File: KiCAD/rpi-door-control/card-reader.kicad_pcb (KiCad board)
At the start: 2 copper layers, 62 x 15 mm, 7 parts, among them P5 CONN_4, P7 CONN_6, U1 BUZZER

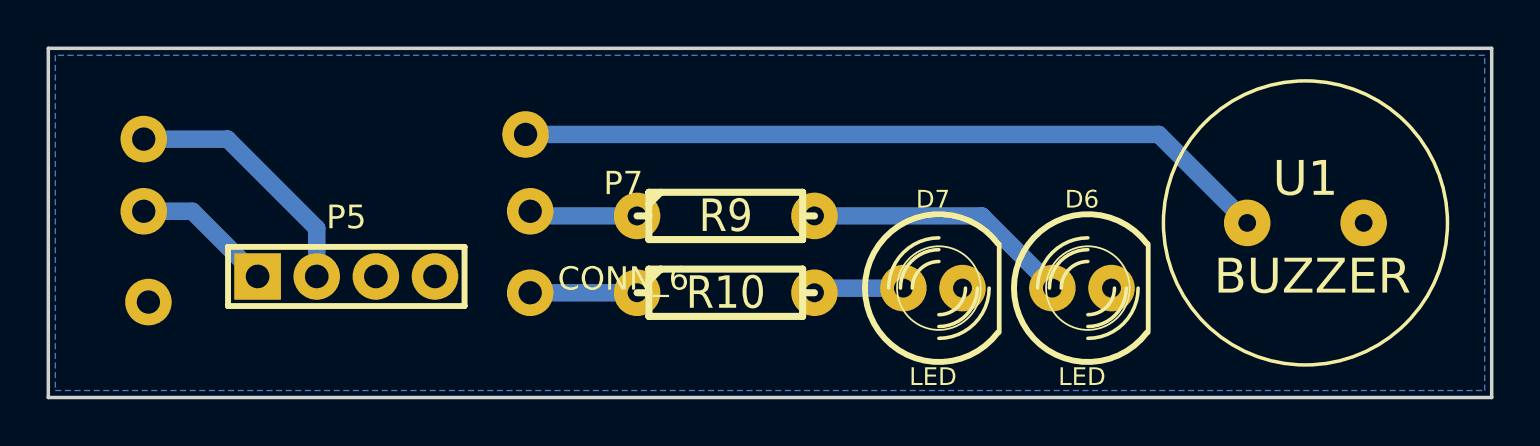
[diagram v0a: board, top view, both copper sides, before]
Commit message: cleaned up wire holes footprint
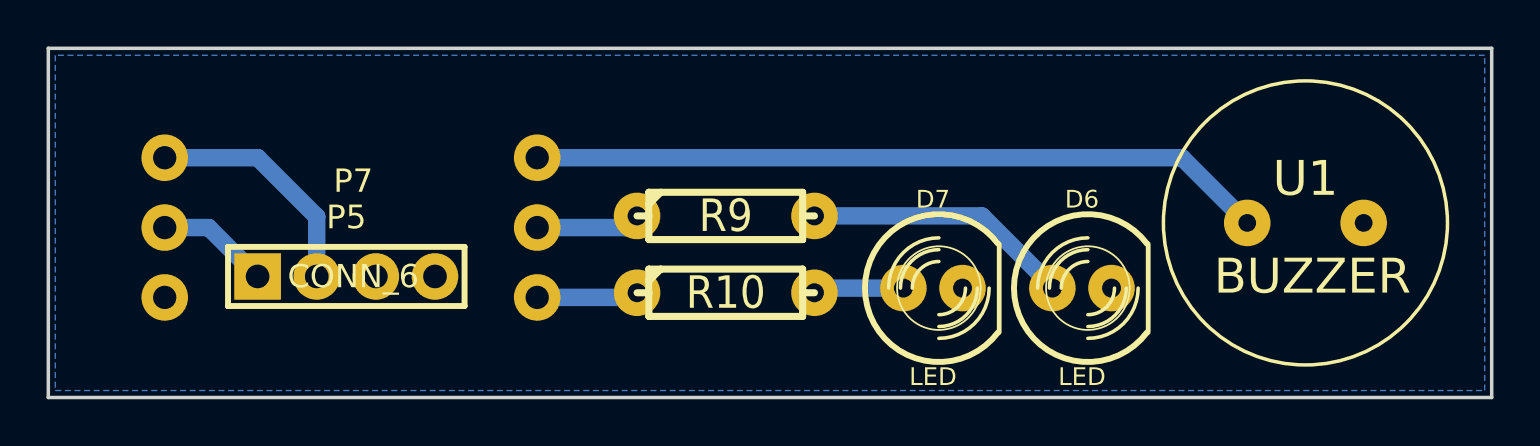
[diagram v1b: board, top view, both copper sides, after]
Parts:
- moved P7 11.6 mm to (94.7, 89.2)
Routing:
- net +5V: track 6.05 -> 4.86 mm
- net /RFID TXD: track 11.1 -> 10.1 mm
- net /BELL: track 32.6 -> 31.7 mm
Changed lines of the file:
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@@
     (thickness 1.6)
     (drawings 4)
-    (tracks 15)
+    (tracks 16)
     (zones 0)
     (modules 7)
@@
   (title_block
     (title "Card Reader Board")
-    (rev 0.3)
+    (rev 0.3.1)
     (company SBW)
     (comment 1 "To be used with Parallax serial RFID reader")
@@
     (mod_text_width 0.15)
     (pad_size 2 2)
-    (pad_drill 1.016)
+    (pad_drill 1)
     (pad_to_mask_clearance 0)
     (aux_axis_origin 72.7 73.5)
@@
     )
   )
-  (module WIRE_HOLES_6 (layer F.Cu)
-    (at 106.3 89.3)
-    (fp_text reference P7 (at 0.1 -2) (layer F.SilkS)
-      (effects (font (size 1 1) (thickness 0.15)))
-    )
-    (fp_text value CONN_6 (at 0.1 2.1) (layer F.SilkS)
-      (effects (font (size 1 1) (thickness 0.15)))
-    )
-    (pad 1 thru_hole circle (at -20.5 -0.8) (size 2 2) (drill 1)
-      (layers *.Cu *.Mask F.SilkS)
-      (net 1 +5V)
-    )
-    (pad 2 thru_hole circle (at -3.9 -0.8) (size 2 2) (drill 1)
-      (layers *.Cu *.Mask F.SilkS)
-      (net 4 /RED)
-    )
-    (pad 4 thru_hole circle (at -20.5 -3.9) (size 2 2) (drill 1)
-      (layers *.Cu *.Mask F.SilkS)
-      (net 5 "/RFID TXD")
-    )
-    (pad 3 thru_hole circle (at -3.9 2.7) (size 2 2) (drill 1)
-      (layers *.Cu *.Mask F.SilkS)
-      (net 3 /GREEN)
-    )
-    (pad 6 thru_hole circle (at -20.3 3.1) (size 2 2) (drill 1)
-      (layers *.Cu *.Mask F.SilkS)
-      (net 6 GND)
-    )
-    (pad 5 thru_hole circle (at -4.1 -4.1) (size 2 2) (drill 1)
-      (layers *.Cu *.Mask F.SilkS)
-      (net 2 /BELL)
-    )
-  )
   (module BUZZER_SMALL (layer F.Cu)
     (at 135.7 89)
@@
     )
   )
+  (module WIRE_HOLES_6 (layer F.Cu)
+    (at 94.7 89.2)
+    (fp_text reference P7 (at 0.1 -2) (layer F.SilkS)
+      (effects (font (size 1 1) (thickness 0.15)))
+    )
+    (fp_text value CONN_6 (at 0.1 2.1) (layer F.SilkS)
+      (effects (font (size 1 1) (thickness 0.15)))
+    )
+    (pad 1 thru_hole circle (at -8 0) (size 2 2) (drill 1)
+      (layers *.Cu *.Mask F.SilkS)
+      (net 1 +5V)
+    )
+    (pad 2 thru_hole circle (at 8 0) (size 2 2) (drill 1)
+      (layers *.Cu *.Mask F.SilkS)
+      (net 4 /RED)
+    )
+    (pad 4 thru_hole circle (at -8 -3) (size 2 2) (drill 1)
+      (layers *.Cu *.Mask F.SilkS)
+      (net 5 "/RFID TXD")
+    )
+    (pad 3 thru_hole circle (at 8 3) (size 2 2) (drill 1)
+      (layers *.Cu *.Mask F.SilkS)
+      (net 3 /GREEN)
+    )
+    (pad 6 thru_hole circle (at -8 3) (size 2 2) (drill 1)
+      (layers *.Cu *.Mask F.SilkS)
+      (net 6 GND)
+    )
+    (pad 5 thru_hole circle (at 8 -3) (size 2 2) (drill 1)
+      (layers *.Cu *.Mask F.SilkS)
+      (net 2 /BELL)
+    )
+  )
   (gr_line (start 81.7 96.5) (end 81.7 81.5) (angle 90) (layer Edge.Cuts) (width 0.15))
   (gr_line (start 143.7 96.5) (end 81.7 96.5) (angle 90) (layer Edge.Cuts) (width 0.15))
   (gr_line (start 143.7 81.5) (end 143.7 96.5) (angle 90) (layer Edge.Cuts) (width 0.15))
   (gr_line (start 81.7 81.5) (end 143.7 81.5) (angle 90) (layer Edge.Cuts) (width 0.15))
-  (segment (start 85.8 88.5) (end 87.89 88.5) (width 0.75) (layer B.Cu) (net 1))
-  (segment (start 87.89 88.5) (end 90.69 91.3) (width 0.75) (layer B.Cu) (net 1))
-  (segment (start 102.2 85.2) (end 129.4 85.2) (width 0.75) (layer B.Cu) (net 2) (status 400000))
-  (segment (start 129.4 85.2) (end 133.2 89) (width 0.75) (layer B.Cu) (net 2) (status 800000))
-  (segment (start 106.99 92) (end 102.4 92) (width 0.75) (layer B.Cu) (net 3) (status C00000))
-  (segment (start 106.99 88.7) (end 102.6 88.7) (width 0.75) (layer B.Cu) (net 4) (status C00000))
-  (segment (start 102.6 88.7) (end 102.4 88.5) (width 0.75) (layer B.Cu) (net 4) (status C00000))
-  (segment (start 93.23 91.3) (end 93.23 89.23) (width 0.75) (layer B.Cu) (net 5))
-  (segment (start 89.4 85.4) (end 85.8 85.4) (width 0.75) (layer B.Cu) (net 5))
-  (segment (start 93.23 89.23) (end 89.4 85.4) (width 0.75) (layer B.Cu) (net 5))
-  (segment (start 118.43 91.8) (end 114.81 91.8) (width 0.75) (layer B.Cu) (net 7) (status C00000))
-  (segment (start 114.81 91.8) (end 114.61 92) (width 0.75) (layer B.Cu) (net 7) (status C00000))
-  (segment (start 124.83 91.8) (end 124.83 91.73) (width 0.75) (layer B.Cu) (net 8) (status C00000))
-  (segment (start 121.8 88.7) (end 114.61 88.7) (width 0.75) (layer B.Cu) (net 8) (status 800000))
-  (segment (start 124.83 91.73) (end 121.8 88.7) (width 0.75) (layer B.Cu) (net 8) (status 400000))
+  (segment (start 86.7 89.2) (end 88.59 89.2) (width 0.75) (layer B.Cu) (net 1))
+  (segment (start 88.59 89.2) (end 90.69 91.3) (width 0.75) (layer B.Cu) (net 1))
+  (segment (start 102.7 86.2) (end 130.4 86.2) (width 0.75) (layer B.Cu) (net 2))
+  (segment (start 130.4 86.2) (end 133.2 89) (width 0.75) (layer B.Cu) (net 2))
+  (segment (start 102.7 92.2) (end 106.79 92.2) (width 0.75) (layer B.Cu) (net 3))
+  (segment (start 106.79 92.2) (end 106.99 92) (width 0.75) (layer B.Cu) (net 3))
+  (segment (start 102.7 89.2) (end 106.49 89.2) (width 0.75) (layer B.Cu) (net 4))
+  (segment (start 106.49 89.2) (end 106.99 88.7) (width 0.75) (layer B.Cu) (net 4))
+  (segment (start 86.7 86.2) (end 90.7 86.2) (width 0.75) (layer B.Cu) (net 5))
+  (segment (start 93.23 88.73) (end 93.23 91.3) (width 0.75) (layer B.Cu) (net 5))
+  (segment (start 90.7 86.2) (end 93.23 88.73) (width 0.75) (layer B.Cu) (net 5))
+  (segment (start 118.43 91.8) (end 114.81 91.8) (width 0.75) (layer B.Cu) (net 7))
+  (segment (start 114.81 91.8) (end 114.61 92) (width 0.75) (layer B.Cu) (net 7))
+  (segment (start 124.83 91.8) (end 124.83 91.73) (width 0.75) (layer B.Cu) (net 8))
+  (segment (start 121.8 88.7) (end 114.61 88.7) (width 0.75) (layer B.Cu) (net 8))
+  (segment (start 124.83 91.73) (end 121.8 88.7) (width 0.75) (layer B.Cu) (net 8))
   (zone (net 6) (net_name GND) (layer B.Cu) (hatch edge 0.508)
     (connect_pads (clearance 1))
